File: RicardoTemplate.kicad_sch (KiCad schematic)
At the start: 37 parts, among them J1 RBUS, U1 ESP32-S3, Y1 40MHz±10ppm

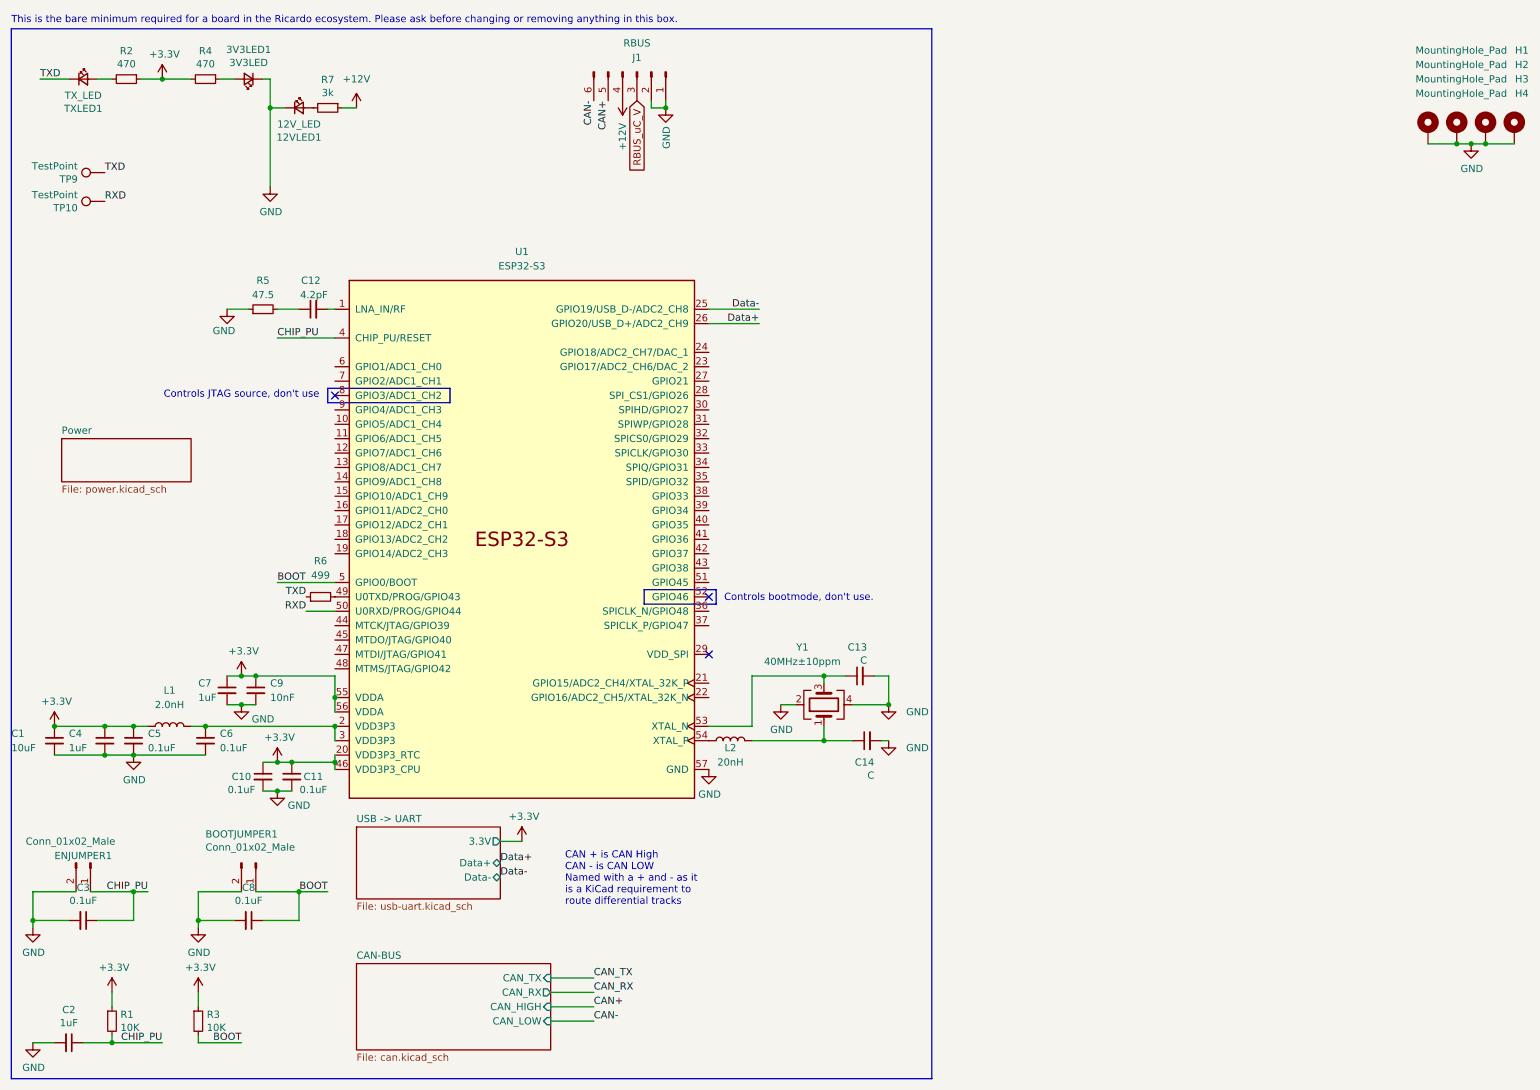
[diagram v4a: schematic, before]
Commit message: implemented fixes that were changed for ordering of nimbus flight electronics, tidied up layout and set up manufacturing constraints
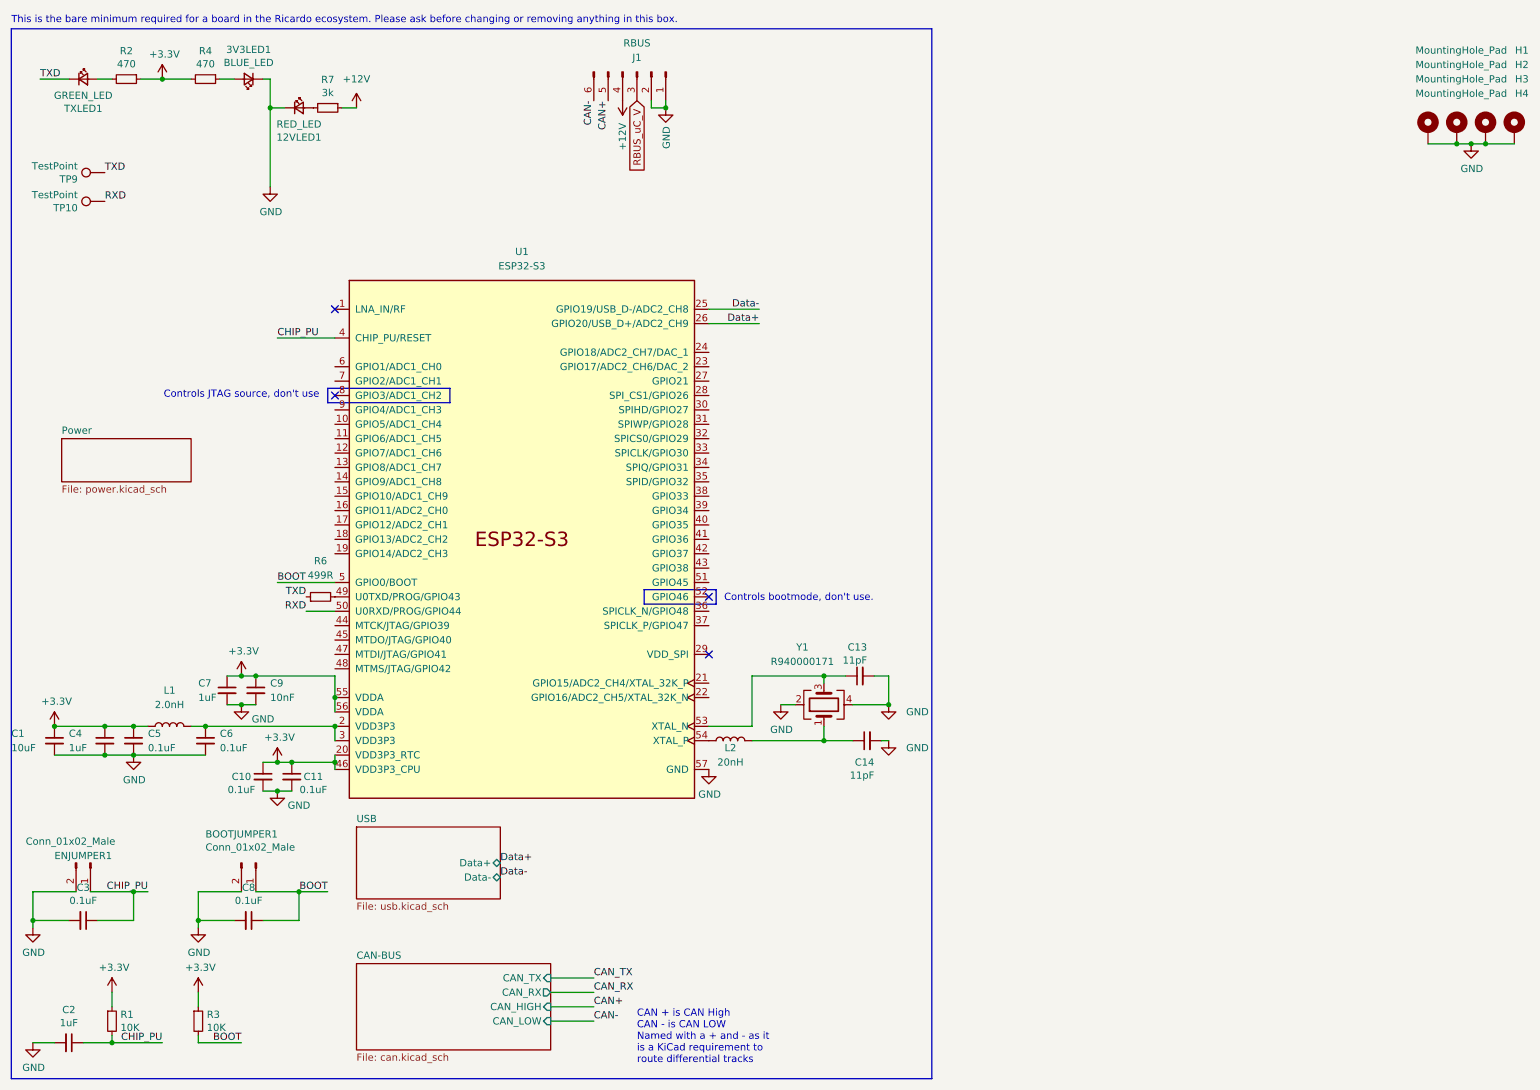
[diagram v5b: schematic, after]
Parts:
- removed C12: 4.2pF, Capacitor_SMD:C_0402_1005Metric, symbol Device:C_Small
- removed R5: 47.5, Resistor_SMD:R_0402_1005Metric, symbol Device:R_Small
- 12VLED1: value 12V_LED -> RED_LED
- 3V3LED1: value 3V3LED -> BLUE_LED
- C13, C14: value C -> 11pF
- R6: value 499 -> 499R
- TXLED1: value TX_LED -> GREEN_LED
- Y1: value 40MHz±10ppm -> R940000171
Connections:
- no-connect marks 3 -> 4
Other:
- sheet USB -> UART renamed USB
- sheet USB: file usb-uart.kicad_sch -> usb.kicad_sch
- sheet USB ports: added none; removed 3.3V
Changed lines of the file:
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@@
   )
   (no_connect (at 69.85 77.47))
+  (no_connect (at 69.85 62.23))
   (no_connect (at 135.89 113.03))
   (no_connect (at 135.89 123.19))
@@
     (stroke (width 0) (type default))
   )
-  (wire (pts (xy 68.58 62.23) (xy 69.85 62.23))
-    (stroke (width 0) (type default))
-  )
   (wire (pts (xy 27.94 21.59) (xy 30.48 21.59))
     (stroke (width 0) (type default))
@@
     (stroke (width 0) (type default))
   )
-  (wire (pts (xy 50.8 62.23) (xy 54.61 62.23))
-    (stroke (width 0) (type default))
-  )
-  (wire (pts (xy 59.69 62.23) (xy 63.5 62.23))
-    (stroke (width 0) (type default))
-  )
   (wire (pts (xy 278.13 33.02) (xy 273.05 33.02))
     (stroke (width 0) (type default))
@@
   )
   (wire (pts (xy 143.51 127) (xy 156.21 127))
-    (stroke (width 0) (type default))
-  )
-  (wire (pts (xy 99.06 156.21) (xy 102.87 156.21))
     (stroke (width 0) (type default))
   )
@@
   )
   (text "CAN + is CAN High\nCAN - is CAN LOW\nNamed with a + and - as it\nis a KiCad requirement to\nroute differential tracks\n"
-    (at 110.49 167.64 0)
+    (at 123.19 195.58 0)
     (effects (font (size 1.27 1.27)) (justify left bottom))
   )
@@
       (effects (font (size 1.27 1.27)))
     )
-    (property "Value" "TX_LED" (at 25.4 24.4856 0)
+    (property "Value" "GREEN_LED" (at 25.4 24.4856 0)
       (effects (font (size 1.27 1.27)))
     )
@@
       (effects (font (size 1.27 1.27)))
     )
-    (property "Value" "3V3LED" (at 54.61 18.6944 0)
+    (property "Value" "BLUE_LED" (at 54.61 18.6944 0)
       (effects (font (size 1.27 1.27)))
     )
@@
         (path "/7db990e4-92e1-4f99-b4d2-435bbec1ba83"
           (reference "BOOTJUMPER1") (unit 1)
-        )
-      )
-    )
-  )
-  (symbol (lib_id "power:+3.3V") (at 102.87 156.21 0) (unit 1)
-    (in_bom yes) (on_board yes) (dnp no)
-    (property "Reference" "#PWR016" (at 102.87 160.02 0)
-      (effects (font (size 1.27 1.27)) hide)
-    )
-    (property "Value" "+3.3V" (at 103.251 151.8158 0)
-      (effects (font (size 1.27 1.27)))
-    )
-    (property "Footprint" "" (at 102.87 156.21 0)
-      (effects (font (size 1.27 1.27)) hide)
-    )
-    (property "Datasheet" "" (at 102.87 156.21 0)
-      (effects (font (size 1.27 1.27)) hide)
-    )
-    (pin "1")
-    (instances
-      (project "RicardoTemplate"
-        (path "/7db990e4-92e1-4f99-b4d2-435bbec1ba83"
-          (reference "#PWR016") (unit 1)
         )
       )
@@
       (effects (font (size 1.27 1.27)))
     )
-    (property "Value" "12V_LED" (at 63.5 29.5656 0)
+    (property "Value" "RED_LED" (at 63.5 29.5656 0)
       (effects (font (size 1.27 1.27)))
     )
@@
       (effects (font (size 1.27 1.27)) (justify left))
     )
-    (property "Value" "C" (at 165.1 144.5514 90)
+    (property "Value" "11pF" (at 165.1 144.5514 90)
       (effects (font (size 1.27 1.27)) (justify left))
     )
@@
       (effects (font (size 1.27 1.27)) (justify left))
     )
-    (property "Value" "C" (at 163.83 124.2314 90)
+    (property "Value" "11pF" (at 163.83 124.2314 90)
       (effects (font (size 1.27 1.27)) (justify left))
     )
@@
         (path "/7db990e4-92e1-4f99-b4d2-435bbec1ba83"
           (reference "TP10") (unit 1)
-        )
-      )
-    )
-  )
-  (symbol (lib_id "Device:C_Small") (at 66.04 62.23 90) (unit 1)
-    (in_bom yes) (on_board yes) (dnp no)
-    (property "Reference" "C12" (at 67.31 57.15 90)
-      (effects (font (size 1.27 1.27)) (justify left))
-    )
-    (property "Value" "4.2pF" (at 68.58 59.69 90)
-      (effects (font (size 1.27 1.27)) (justify left))
-    )
-    (property "Footprint" "Capacitor_SMD:C_0402_1005Metric" (at 66.04 62.23 0)
-      (effects (font (size 1.27 1.27)) hide)
-    )
-    (property "Datasheet" "~" (at 66.04 62.23 0)
-      (effects (font (size 1.27 1.27)) hide)
-    )
-    (pin "1")
-    (pin "2")
-    (instances
-      (project "RicardoTemplate"
-        (path "/7db990e4-92e1-4f99-b4d2-435bbec1ba83"
-          (reference "C12") (unit 1)
         )
       )
@@
       (effects (font (size 1.27 1.27)))
     )
-    (property "Value" "40MHz±10ppm" (at 152.4 124.46 90)
+    (property "Value" "R940000171" (at 152.4 124.46 90)
       (effects (font (size 1.27 1.27)))
     )
@@
     )
   )
-  (symbol (lib_id "power:GND") (at 50.8 62.23 0) (unit 1)
-    (in_bom yes) (on_board yes) (dnp no)
-    (property "Reference" "#PWR09" (at 50.8 68.58 0)
-      (effects (font (size 1.27 1.27)) hide)
-    )
-    (property "Value" "GND" (at 48.26 66.04 0)
-      (effects (font (size 1.27 1.27)) (justify left))
-    )
-    (property "Footprint" "" (at 50.8 62.23 0)
-      (effects (font (size 1.27 1.27)) hide)
-    )
-    (property "Datasheet" "" (at 50.8 62.23 0)
-      (effects (font (size 1.27 1.27)) hide)
-    )
-    (pin "1")
-    (instances
-      (project "RicardoTemplate"
-        (path "/7db990e4-92e1-4f99-b4d2-435bbec1ba83"
-          (reference "#PWR09") (unit 1)
-        )
-      )
-    )
-  )
   (symbol (lib_id "Device:R_Small") (at 67.31 113.03 90) (unit 1)
     (in_bom yes) (on_board yes) (dnp no)
@@
       (effects (font (size 1.27 1.27)))
     )
-    (property "Value" "499" (at 67.31 109.22 90)
+    (property "Value" "499R" (at 67.31 109.22 90)
       (effects (font (size 1.27 1.27)))
     )
@@
         (path "/7db990e4-92e1-4f99-b4d2-435bbec1ba83"
           (reference "R6") (unit 1)
-        )
-      )
-    )
-  )
-  (symbol (lib_id "Device:R_Small") (at 57.15 62.23 90) (unit 1)
-    (in_bom yes) (on_board yes) (dnp no)
-    (property "Reference" "R5" (at 57.15 57.15 90)
-      (effects (font (size 1.27 1.27)))
-    )
-    (property "Value" "47.5" (at 57.15 59.69 90)
-      (effects (font (size 1.27 1.27)))
-    )
-    (property "Footprint" "Resistor_SMD:R_0402_1005Metric" (at 57.15 62.23 0)
-      (effects (font (size 1.27 1.27)) hide)
-    )
-    (property "Datasheet" "~" (at 57.15 62.23 0)
-      (effects (font (size 1.27 1.27)) hide)
-    )
-    (pin "1")
-    (pin "2")
-    (instances
-      (project "RicardoTemplate"
-        (path "/7db990e4-92e1-4f99-b4d2-435bbec1ba83"
-          (reference "R5") (unit 1)
         )
       )
@@
     (stroke (width 0) (type solid))
     (fill (color 0 0 0 0.0000))
-    (property "Sheetname" "USB -> UART" (at 73.66 152.9584 0)
+    (property "Sheetname" "USB" (at 73.66 152.9584 0)
       (effects (font (size 1.27 1.27)) (justify left bottom))
     )
-    (property "Sheetfile" "usb-uart.kicad_sch" (at 73.66 166.9546 0)
+    (property "Sheetfile" "usb.kicad_sch" (at 73.66 166.9546 0)
       (effects (font (size 1.27 1.27)) (justify left top))
     )
-    (pin "3.3V" output (at 99.06 156.21 0)
-      (effects (font (size 1.27 1.27)) (justify right))
-    )
     (pin "Data+" bidirectional (at 99.06 160.02 0)

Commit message: esp32 s3 better footprint
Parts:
- U1: footprint Package_DFN_QFN:QFN-56-1EP_7x7mm_P0.4mm_EP5.6x5.6mm -> iclr:QFN40P700X700X90-57N
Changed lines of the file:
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@@
       (effects (font (size 1.27 1.27)))
     )
-    (property "Footprint" "Package_DFN_QFN:QFN-56-1EP_7x7mm_P0.4mm_EP5.6x5.6mm" (at 102.87 153.67 0)
+    (property "Footprint" "iclr:QFN40P700X700X90-57N" (at 102.87 153.67 0)
       (effects (font (size 1.27 1.27)) hide)
     )

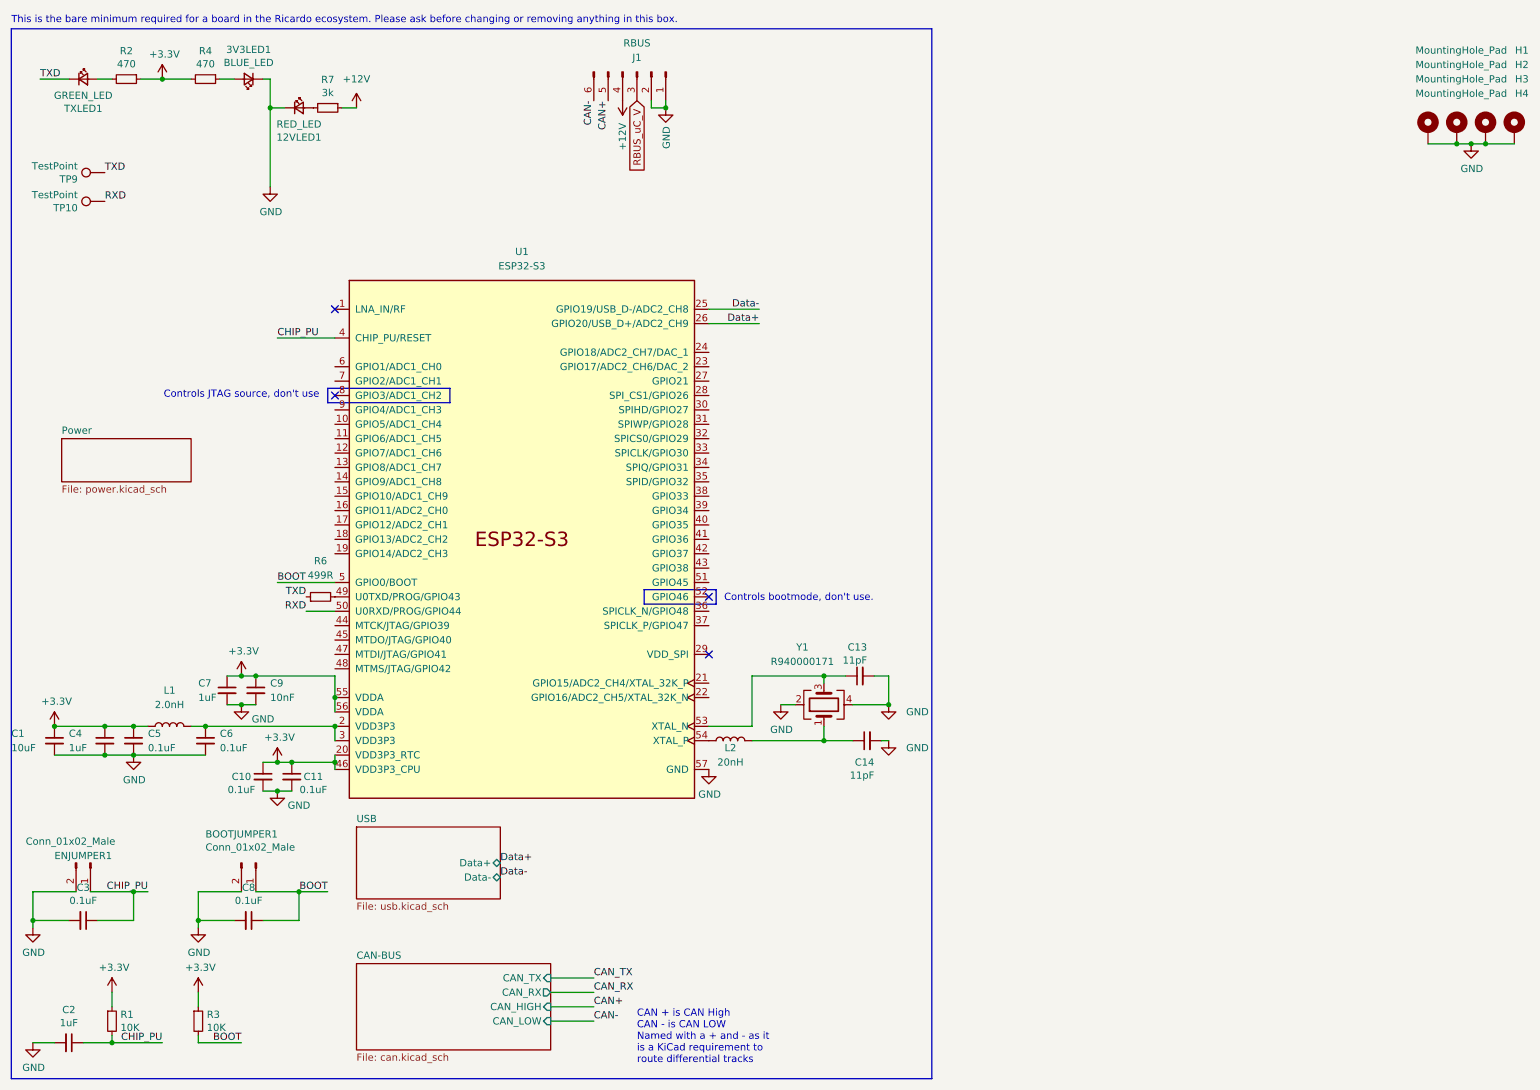
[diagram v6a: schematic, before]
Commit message: Added CAN LEDs and some general fixes noticed over the year
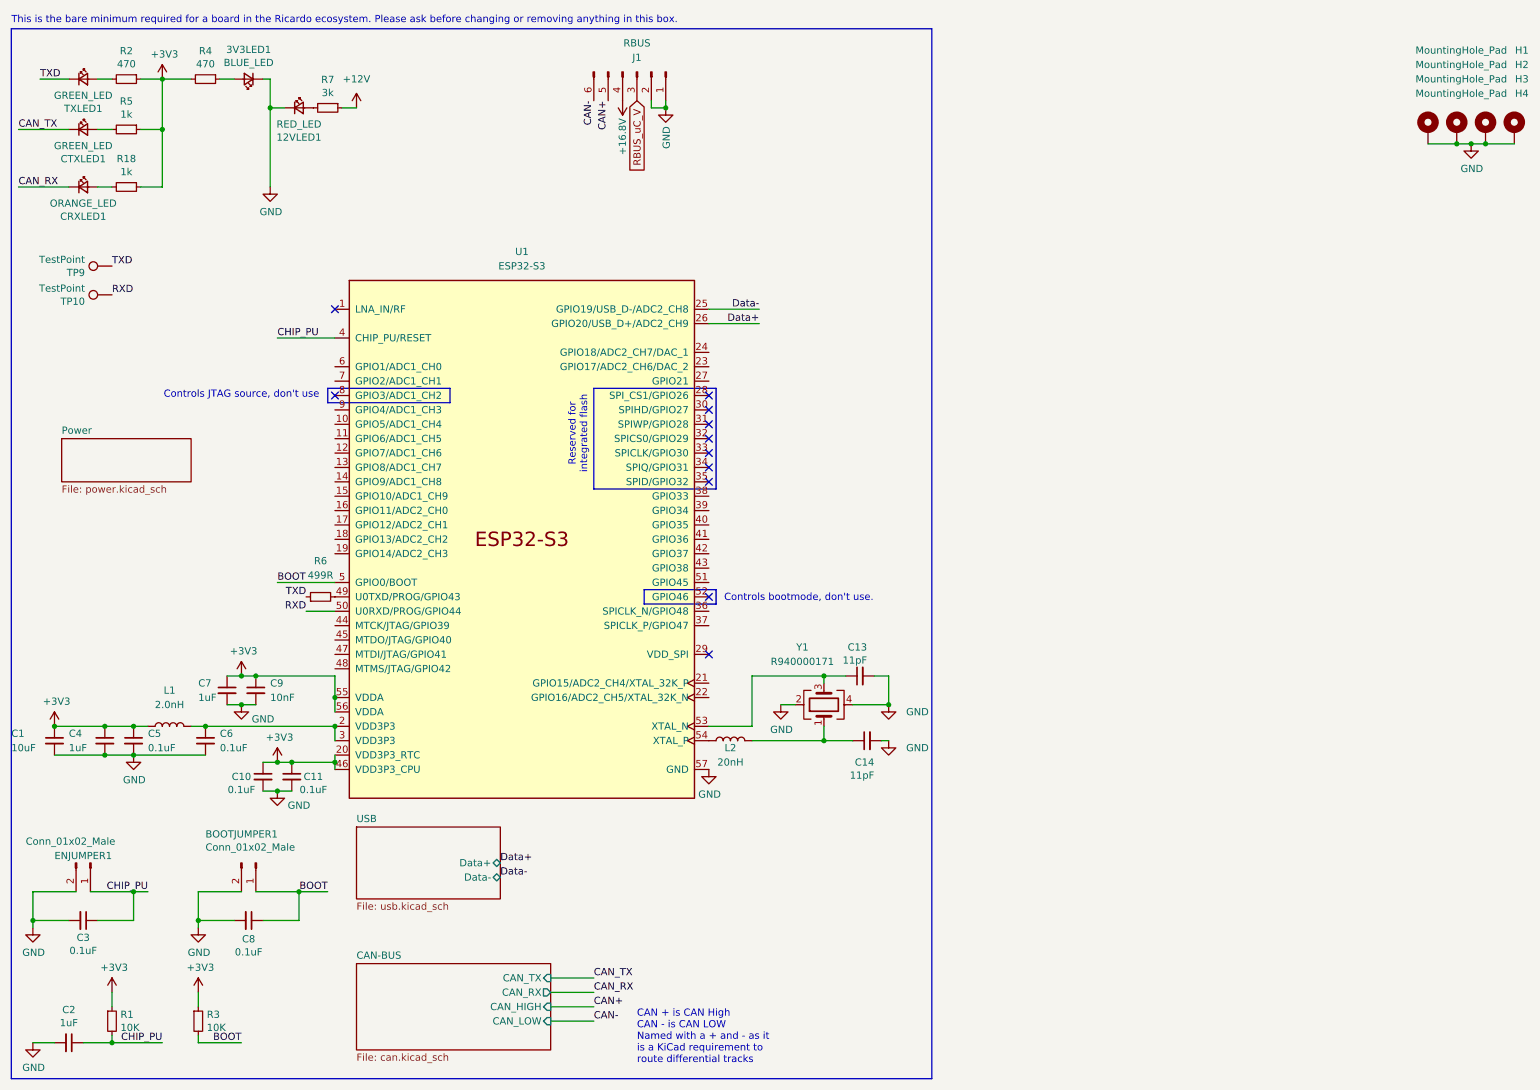
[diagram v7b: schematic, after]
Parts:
- added CRXLED1: ORANGE_LED, Resistor_SMD:R_0402_1005Metric, symbol Device:LED_Small
- added CTXLED1: GREEN_LED, Resistor_SMD:R_0402_1005Metric, symbol Device:LED_Small
- added R18, R5: 1k, Resistor_SMD:R_0402_1005Metric, symbol Device:R_Small
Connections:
- net +12V: no longer J1.4 (Pin_4)
- net +3V3: now also R18.1, R5.1
- net CAN_RX: now also CRXLED1.1 (K)
- net CAN_TX: now also CTXLED1.1 (K)
- new net: CTXLED1.2 (A), R5.2
- new net: CRXLED1.2 (A), R18.2
- new net +16.8V: J1.4 (Pin_4)
- no-connect marks 4 -> 11
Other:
- note added: "Reserved for integrated flash"
- moved on the sheet: TP10, TP9

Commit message: Changed minifit Jr footprint to horizontal
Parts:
- J1: footprint Connector_Molex:Molex_Mini-Fit_Jr_5566-06A_2x03_P4.20mm_Vertical -> Connector_Molex:Molex_Mini-Fit_Jr_5569-06A2_2x03_P4.20mm_Horizontal
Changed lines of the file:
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@@
 			)
 		)
-		(property "Footprint" "Connector_Molex:Molex_Mini-Fit_Jr_5566-06A_2x03_P4.20mm_Vertical"
+		(property "Footprint" "Connector_Molex:Molex_Mini-Fit_Jr_5569-06A2_2x03_P4.20mm_Horizontal"
 			(at 123.19 20.32 0)
 			(effects
